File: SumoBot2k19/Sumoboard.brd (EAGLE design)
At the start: 80 x 60 mm, 38 parts

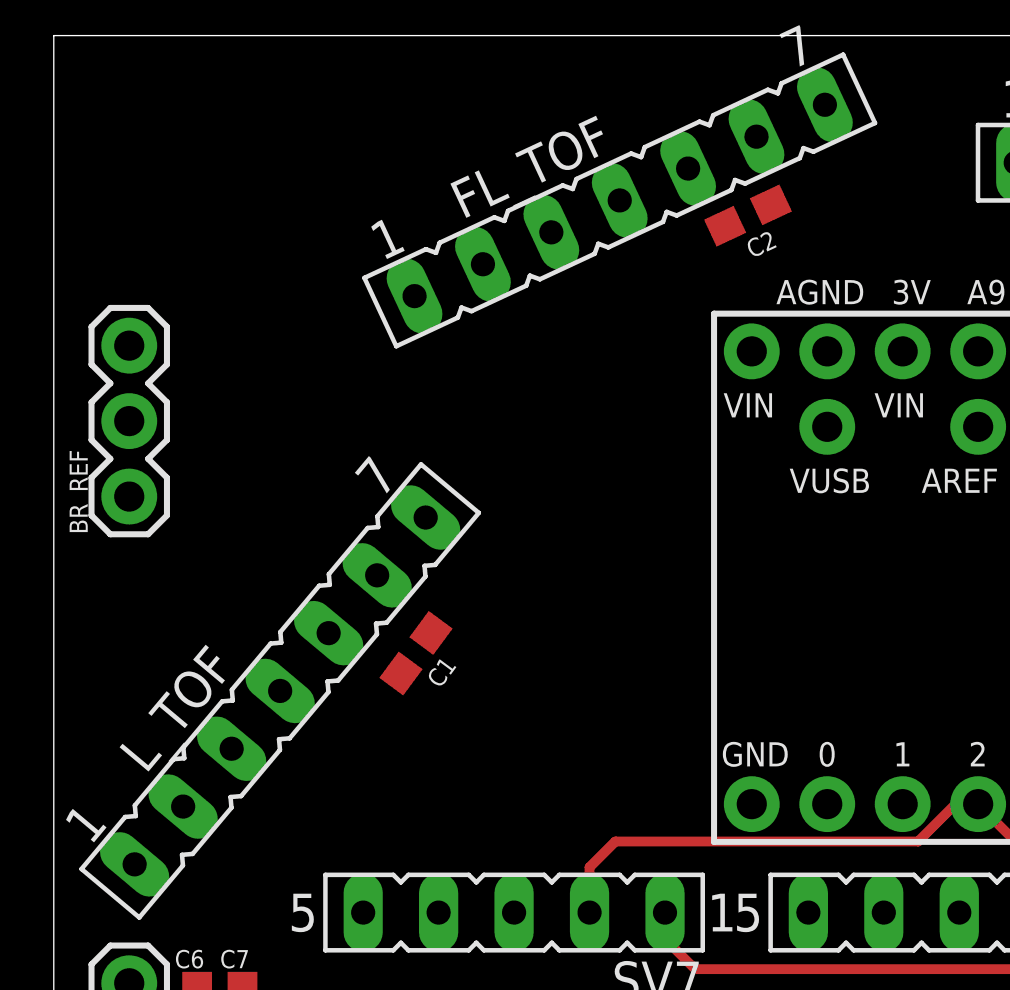
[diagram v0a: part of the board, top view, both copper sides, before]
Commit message: More connections
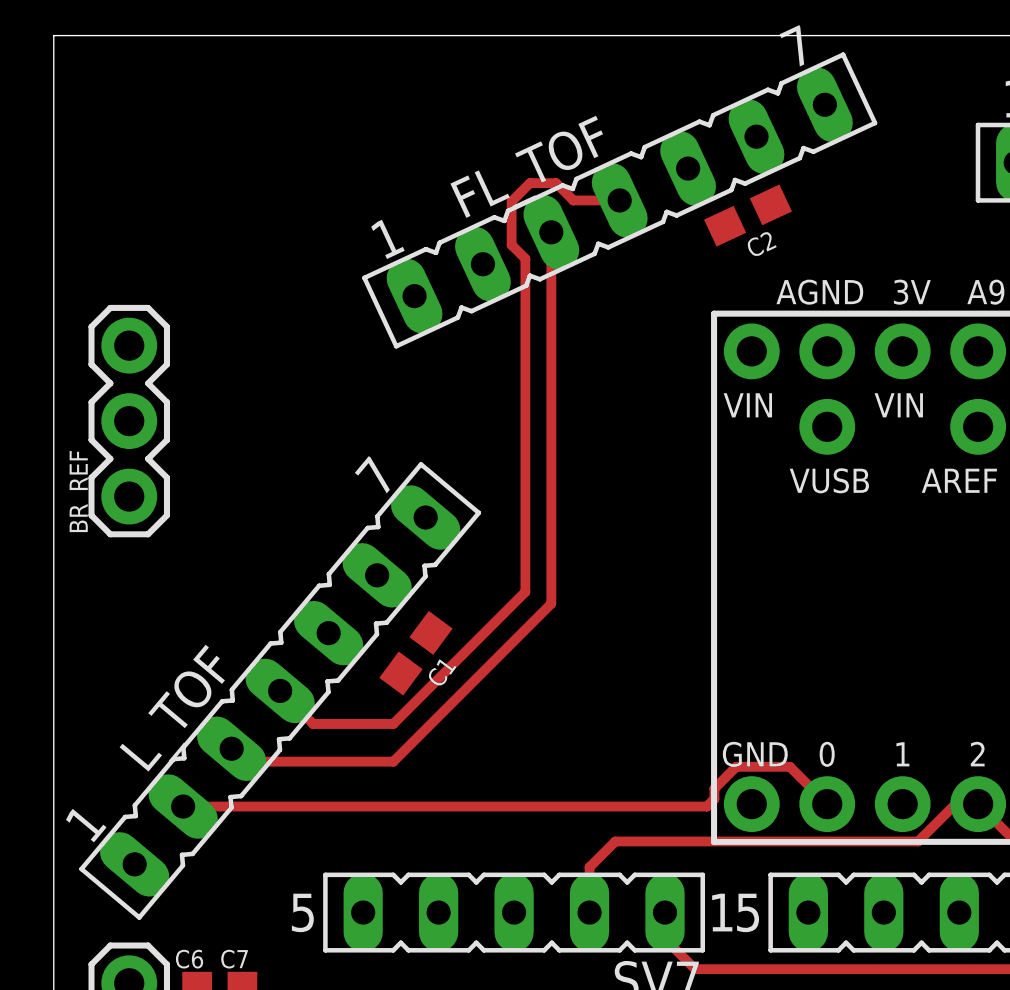
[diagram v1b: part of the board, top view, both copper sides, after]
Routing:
- net SDA: track 0.00 -> 28.0 mm
- net SCL: track 0.00 -> 25.6 mm
- net XSHUT_L: track 0.00 -> 23.0 mm
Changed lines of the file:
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@@
 <wire x1="67.22553125" y1="44.45000625" x2="68.75761875" y2="45.7355875" width="0.001" layer="49"/>
 <wire x1="52.2286" y1="57.25985625" x2="53.073840625" y2="59.072475" width="0.001" layer="49"/>
-<wire x1="27.7714" y1="57.25985625" x2="11.65725" y2="49.74570625" width="0.001" layer="49"/>
 <wire x1="80" y1="60.000003125" x2="80" y2="0" width="0.001" layer="49"/>
 <wire x1="0" y1="60.000003125" x2="0" y2="0" width="0.001" layer="49"/>
@@
 <wire x1="0" y1="0" x2="80" y2="0" width="0.001" layer="49"/>
 <wire x1="67.22553125" y1="44.45000625" x2="78.654290625" y2="30.8297375" width="0.001" layer="49"/>
-<wire x1="11.65725" y1="49.74570625" x2="10.812009375" y2="51.558315625" width="0.001" layer="49"/>
-<wire x1="12.77446875" y1="44.45000625" x2="1.345709375" y2="30.8297375" width="0.001" layer="49"/>
-<wire x1="1.345709375" y1="30.8297375" x2="-0.18638125" y2="22.115309375" width="0.001" layer="49"/>
 <wire x1="31.11" y1="55.00000625" x2="31.11" y2="57.00000625" width="0.001" layer="49"/>
 <wire x1="31.11" y1="55.00000625" x2="48.89" y2="55.00000625" width="0.001" layer="49"/>
@@
 <wire x1="63.762359375" y1="49.772778125" x2="65.310040625" y2="52.049103125" width="0" layer="19" extent="1-1"/>
 <wire x1="56.515" y1="39.21000625" x2="63.762359375" y2="49.772778125" width="0" layer="19" extent="1-1"/>
-<wire x1="73.7582625" y1="32.77223125" x2="56.515" y2="39.21000625" width="0" layer="19" extent="1-1"/>
-<wire x1="75.645359375" y1="34.0485" x2="73.7582625" y2="32.77223125" width="0" layer="19" extent="1-1"/>
+<wire x1="75.645359375" y1="34.0485" x2="77.47" y2="51.65600625" width="0" layer="19" extent="1-1"/>
+<wire x1="73.7582625" y1="32.77223125" x2="75.645359375" y2="34.0485" width="0" layer="19" extent="1-1"/>
 <wire x1="77.47" y1="14.82600625" x2="73.7582625" y2="32.77223125" width="0" layer="19" extent="1-1"/>
 <wire x1="44.538" y1="53.18000625" x2="56.515" y2="39.21000625" width="0" layer="19" extent="1-1"/>
@@
 <contactref element="R_TOF" pad="4"/>
 <contactref element="B1" pad="17"/>
+<wire x1="7.62" y1="37.94000625" x2="8.73000625" y2="36.83" width="0.3302" layer="1"/>
+<wire x1="8.73000625" y1="36.83" x2="11.43" y2="36.83" width="0.3302" layer="1"/>
+<wire x1="11.43" y1="36.83" x2="15.875" y2="41.275" width="0.3302" layer="1"/>
+<wire x1="17.489434375" y1="54.45000625" x2="19.05" y2="54.45000625" width="0.3302" layer="1"/>
+<wire x1="16.906896875" y1="55.03254375" x2="17.489434375" y2="54.45000625" width="0.3302" layer="1"/>
+<wire x1="16.0308625" y1="55.03254375" x2="16.906896875" y2="55.03254375" width="0.3302" layer="1"/>
+<wire x1="15.411415625" y1="54.413096875" x2="16.0308625" y2="55.03254375" width="0.3302" layer="1"/>
+<wire x1="15.411415625" y1="52.951546875" x2="15.411415625" y2="54.413096875" width="0.3302" layer="1"/>
+<wire x1="15.875" y1="52.4879625" x2="15.411415625" y2="52.951546875" width="0.3302" layer="1"/>
+<wire x1="15.875" y1="41.275" x2="15.875" y2="52.4879625" width="0.3302" layer="1"/>
 <wire x1="46.355" y1="49.37000625" x2="60.706" y2="54.19600625" width="0" layer="19" extent="1-1"/>
 <wire x1="39.99991875" y1="55.72000625" x2="46.355" y2="49.37000625" width="0" layer="19" extent="1-1"/>
 <wire x1="72.38" y1="37.94000625" x2="60.706" y2="54.19600625" width="0" layer="19" extent="1-1"/>
 <wire x1="19.05" y1="54.45000625" x2="39.99991875" y2="55.72000625" width="0" layer="19" extent="1-1"/>
-<wire x1="7.62" y1="37.94000625" x2="19.05" y2="54.45000625" width="0" layer="19" extent="1-1"/>
 </signal>
 <signal name="SCL">
@@
 <contactref element="R_TOF" pad="3"/>
 <contactref element="B1" pad="16"/>
+<wire x1="5.98731875" y1="35.994253125" x2="6.421571875" y2="35.56" width="0.3302" layer="1"/>
+<wire x1="6.421571875" y1="35.56" x2="11.43" y2="35.56" width="0.3302" layer="1"/>
+<wire x1="16.747978125" y1="40.877978125" x2="11.43" y2="35.56" width="0.3302" layer="1"/>
+<wire x1="16.747978125" y1="53.376553125" x2="16.747978125" y2="40.877978125" width="0.3302" layer="1"/>
 <wire x1="48.895" y1="49.37000625" x2="58.403978125" y2="55.26945625" width="0" layer="19" extent="1-1"/>
 <wire x1="37.45991875" y1="55.72000625" x2="48.895" y2="49.37000625" width="0" layer="19" extent="1-1"/>
 <wire x1="70.74731875" y1="39.88575625" x2="58.403978125" y2="55.26945625" width="0" layer="19" extent="1-1"/>
 <wire x1="16.747978125" y1="53.376553125" x2="37.45991875" y2="55.72000625" width="0" layer="19" extent="1-1"/>
-<wire x1="5.98731875" y1="35.994253125" x2="16.747978125" y2="53.376553125" width="0" layer="19" extent="1-1"/>
 </signal>
 <signal name="XSHUT_L">
 <contactref element="L_TOF" pad="2"/>
 <contactref element="B1" pad="0"/>
-<wire x1="4.3546375" y1="34.0485" x2="26.035" y2="34.13000625" width="0" layer="19" extent="1-1"/>
+<wire x1="4.3546375" y1="34.0485" x2="21.9835" y2="34.0485" width="0.3302" layer="1"/>
+<wire x1="22.2377" y1="34.6508" x2="22.97420625" y2="35.38730625" width="0.3302" layer="1"/>
+<wire x1="22.2377" y1="34.3027" x2="22.2377" y2="34.6508" width="0.3302" layer="1"/>
+<wire x1="22.97420625" y1="35.38730625" x2="24.7777" y2="35.38730625" width="0.3302" layer="1"/>
+<wire x1="24.7777" y1="35.38730625" x2="26.035" y2="34.13000625" width="0.3302" layer="1"/>
+<wire x1="21.9835" y1="34.0485" x2="22.2377" y2="34.3027" width="0.3302" layer="1"/>
 </signal>
 <signal name="GPIO">

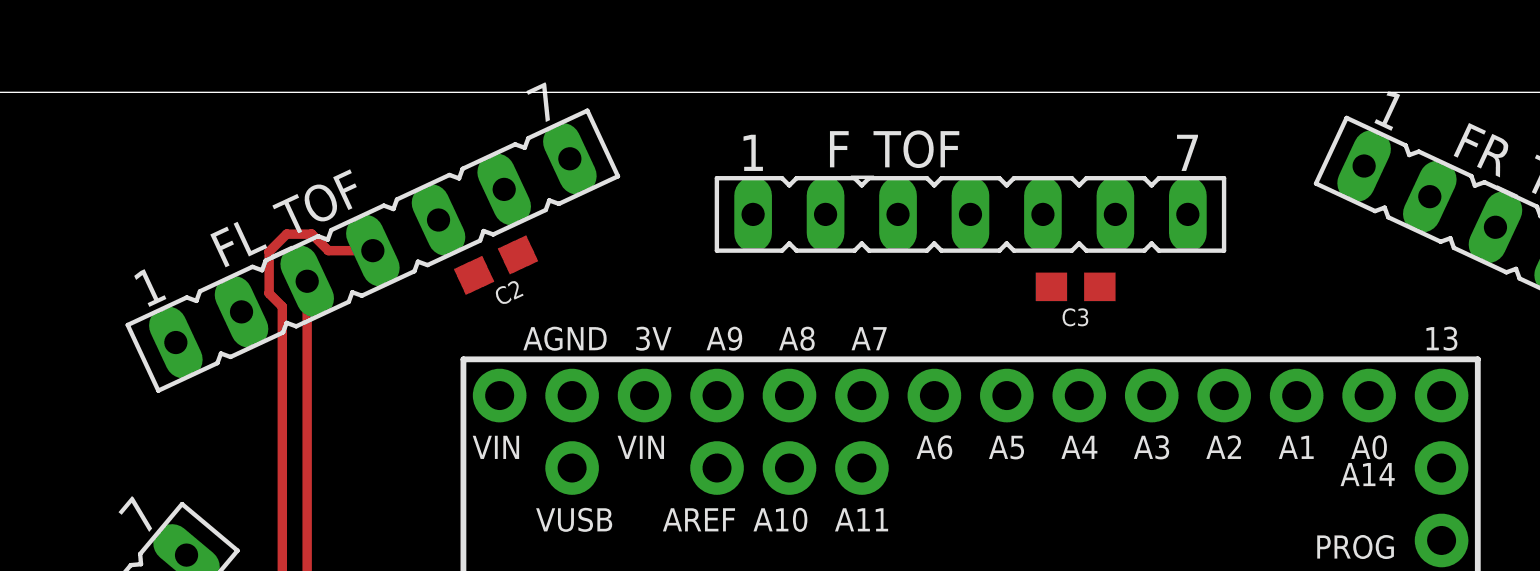
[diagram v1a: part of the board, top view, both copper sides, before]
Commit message: added more routes
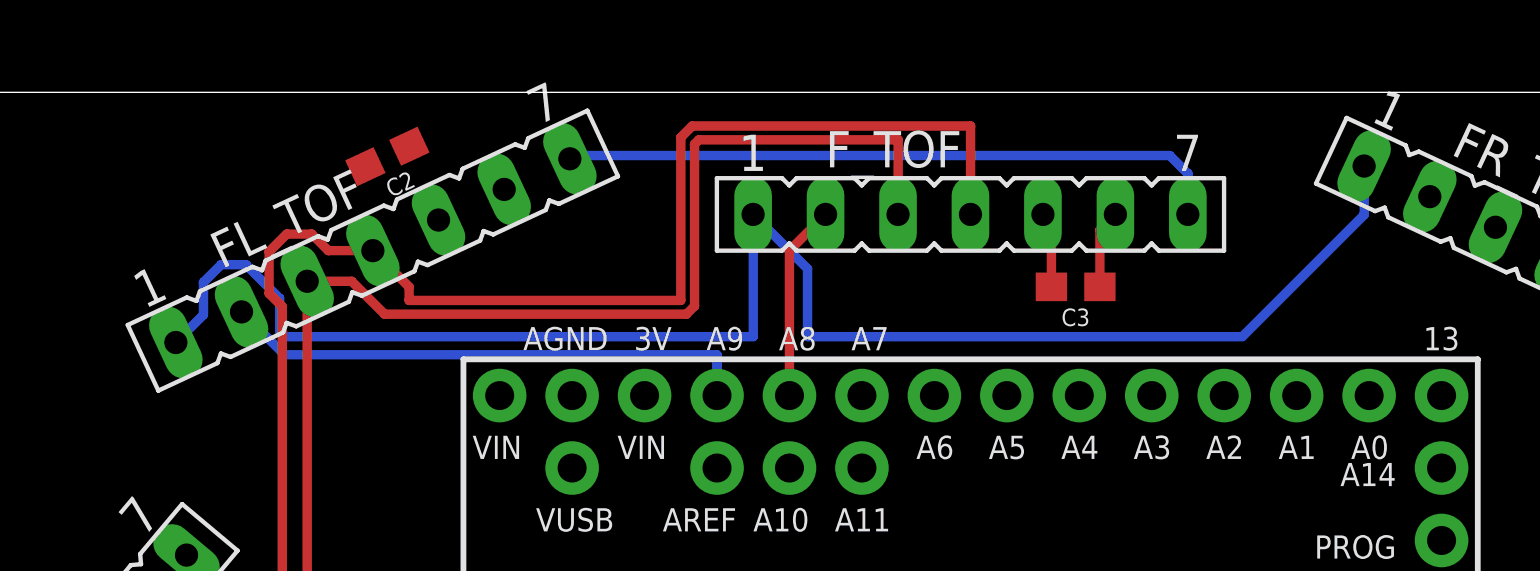
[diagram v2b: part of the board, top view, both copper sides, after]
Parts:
- moved C2 5.39 mm to (19.6, 57.8)
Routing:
- net GPIO: track 0.00 -> 56.1 mm
- net SDA: track 28.0 -> 59.0 mm
- net SCL: track 25.6 -> 55.3 mm
- net VDD: track 0.00 -> 23.4 mm
- net XSHUT_FL: track 0.00 -> 18.7 mm
- net XSHUT_F: track 0.00 -> 6.87 mm
- net 3.3V: track 0.00 -> 2.76 mm
- net GND: track 0.00 -> 2.66 mm

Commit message: connections yeah!
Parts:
- moved C2 3.42 mm to (16.4, 56.5)
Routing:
- net VDD: track 23.4 -> 56.0 mm
- net 3.3V: track 2.76 -> 19.9 mm
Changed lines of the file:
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@@
 <attribute name="VALUE" x="11.58999375" y="21.161996875" size="0.6096" layer="27" font="vector" ratio="20" rot="R180" align="top-center"/>
 </element>
-<element name="C2" library="SparkFun-Capacitors" library_urn="urn:adsk.eagle:library:510" package="0603" package3d_urn="urn:adsk.eagle:package:37414/1" value="0.1uF" x="19.558" y="57.75200625" smashed="yes" rot="R205">
-<attribute name="NAME" x="19.8800375" y="57.0614" size="0.6096" layer="25" font="vector" ratio="20" rot="R205" align="bottom-center"/>
-<attribute name="PROD_ID" value="CAP-08604" x="-50.318628125" y="120.455715625" size="1.778" layer="27" rot="R205" display="off"/>
-<attribute name="VALUE" x="19.235965625" y="58.442615625" size="0.6096" layer="27" font="vector" ratio="20" rot="R205" align="top-center"/>
+<element name="C2" library="SparkFun-Capacitors" library_urn="urn:adsk.eagle:library:510" package="0603" package3d_urn="urn:adsk.eagle:package:37414/1" value="0.1uF" x="16.383" y="56.48200625" smashed="yes" rot="R205">
+<attribute name="NAME" x="16.7050375" y="55.7914" size="0.6096" layer="25" font="vector" ratio="20" rot="R205" align="bottom-center"/>
+<attribute name="PROD_ID" value="CAP-08604" x="-53.493628125" y="119.185715625" size="1.778" layer="27" rot="R205" display="off"/>
+<attribute name="VALUE" x="16.060965625" y="57.172615625" size="0.6096" layer="27" font="vector" ratio="20" rot="R205" align="top-center"/>
 </element>
 <element name="C3" library="SparkFun-Capacitors" library_urn="urn:adsk.eagle:library:510" package="0603" package3d_urn="urn:adsk.eagle:package:37414/1" value="0.1uF" x="43.688" y="53.18000625" smashed="yes" rot="R180">
@@
 <wire x1="45.07991875" y1="55.72000625" x2="44.538" y2="55.1780875" width="0.3302" layer="1"/>
 <wire x1="44.538" y1="55.1780875" x2="44.538" y2="53.18000625" width="0.3302" layer="1"/>
+<wire x1="23.654040625" y1="56.59690625" x2="23.409715625" y2="56.84123125" width="0.3302" layer="1"/>
+<wire x1="23.409715625" y1="56.84123125" x2="17.153359375" y2="56.84123125" width="0.3302" layer="1"/>
+<wire x1="2.54" y1="47.02299375" x2="7.731484375" y2="41.831509375" width="0.3302" layer="1"/>
+<wire x1="7.731484375" y1="41.831509375" x2="10.885359375" y2="41.831509375" width="0.3302" layer="1"/>
 <wire x1="65.310040625" y1="52.049103125" x2="77.47" y2="51.65600625" width="0" layer="19" extent="1-1"/>
 <wire x1="63.762359375" y1="49.772778125" x2="65.310040625" y2="52.049103125" width="0" layer="19" extent="1-1"/>
@@
 <wire x1="28.575" y1="49.37000625" x2="44.538" y2="53.18000625" width="0" layer="19" extent="1-1"/>
 <wire x1="23.654040625" y1="56.59690625" x2="28.575" y2="49.37000625" width="0" layer="19" extent="1-1"/>
-<wire x1="20.328359375" y1="58.11123125" x2="23.654040625" y2="56.59690625" width="0" layer="19" extent="1-1"/>
 <wire x1="12.697596875" y1="39.893284375" x2="28.575" y2="49.37000625" width="0" layer="19" extent="1-1"/>
 <wire x1="10.885359375" y1="41.831509375" x2="12.697596875" y2="39.893284375" width="0" layer="19" extent="1-1"/>
-<wire x1="2.54" y1="47.02299375" x2="10.885359375" y2="41.831509375" width="0" layer="19" extent="1-1"/>
 <wire x1="23.52799375" y1="7.112" x2="12.697596875" y2="39.893284375" width="0" layer="19" extent="1-1"/>
 <wire x1="40.73400625" y1="3.048" x2="23.52799375" y2="7.112" width="0" layer="19" extent="1-1"/>
@@
 <wire x1="42.838" y1="53.18000625" x2="56.515" y2="41.75000625" width="0" layer="19" extent="1-1"/>
 <wire x1="21.35201875" y1="55.52345625" x2="11.6864" y2="38.526725" width="0" layer="19" extent="1-1"/>
-<wire x1="18.7876375" y1="57.392778125" x2="21.35201875" y2="55.52345625" width="0" layer="19" extent="1-1"/>
+<wire x1="15.6126375" y1="56.122778125" x2="21.35201875" y2="55.52345625" width="0" layer="19" extent="1-1"/>
 </signal>
 <signal name="SDA">
@@
 <wire x1="47.625" y1="55.7250875" x2="47.61991875" y2="55.72000625" width="0.3302" layer="16"/>
 <wire x1="26.07070625" y1="57.785" x2="46.99" y2="57.785" width="0.3302" layer="16"/>
+<wire x1="25.9560625" y1="57.67035625" x2="24.807615625" y2="58.818803125" width="0.3302" layer="1"/>
+<wire x1="10.558803125" y1="58.818803125" x2="9.525" y2="57.785" width="0.3302" layer="1"/>
+<wire x1="9.525" y1="57.785" x2="9.525" y2="46.770303125" width="0.3302" layer="1"/>
+<wire x1="9.525" y1="46.770303125" x2="12.518040625" y2="43.7772625" width="0.3302" layer="1"/>
+<wire x1="24.807615625" y1="58.818803125" x2="10.558803125" y2="58.818803125" width="0.3302" layer="1"/>
 <wire x1="47.61991875" y1="55.72000625" x2="67.6120625" y2="50.975653125" width="0" layer="19" extent="1-1"/>
-<wire x1="12.518040625" y1="43.7772625" x2="25.9560625" y2="57.67035625" width="0" layer="19" extent="1-1"/>
 <wire x1="77.278040625" y1="32.102746875" x2="67.6120625" y2="50.975653125" width="0" layer="19" extent="1-1"/>
 </signal>
